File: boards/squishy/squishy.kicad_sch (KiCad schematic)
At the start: 66 parts, among them J10 QXH-060, J2 Conn_02x20_Odd_Even_Shielded, J8 TRIGGER, J9 REFCLK, SW2 DFU, U1 LFE5UM5G-45F-8BG381C, U2 W25N01GVZEIG, U6 ATSAMD09D14A-M, X1 48MHz

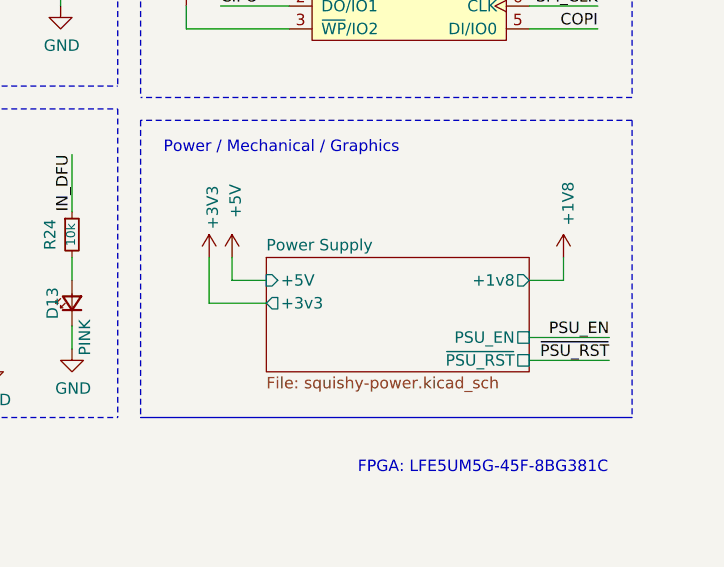
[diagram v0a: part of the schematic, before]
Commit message: hardware: squishy: some more cleanup, as well as starting work on the PSU side of things finally
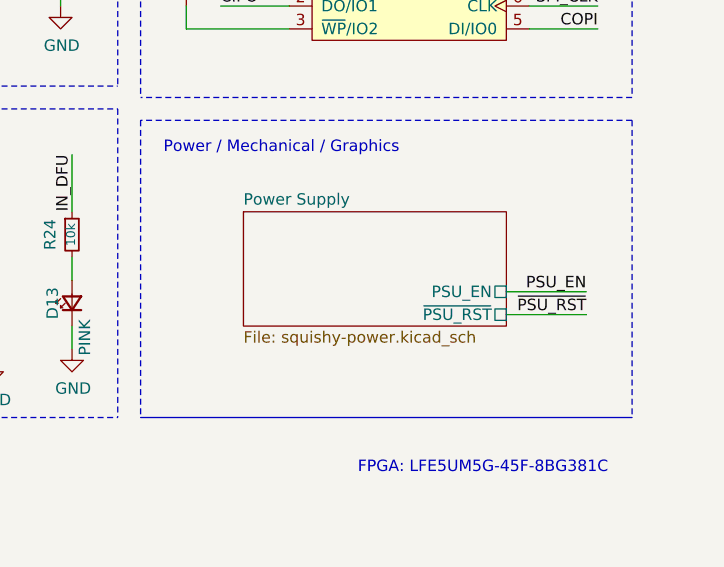
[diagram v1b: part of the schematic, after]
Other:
- sheet Power Supply ports: added none; removed +1v8, +3v3, +5V
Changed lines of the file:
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@@
     (stroke (width 0) (type default) (color 0 0 0 0))
   )
-  (wire (pts (xy 365.76 237.49) (xy 359.41 237.49))
-    (stroke (width 0) (type solid) (color 0 0 0 0))
-  )
   (wire (pts (xy 212.09 257.81) (xy 209.55 257.81))
     (stroke (width 0) (type default) (color 0 0 0 0))
@@
     (stroke (width 0) (type default) (color 0 0 0 0))
   )
-  (wire (pts (xy 361.95 234.95) (xy 365.76 234.95))
-    (stroke (width 0) (type solid) (color 0 0 0 0))
-  )
   (wire (pts (xy 209.55 260.35) (xy 209.55 265.43))
     (stroke (width 0) (type default) (color 0 0 0 0))
@@
     (stroke (width 0) (type default) (color 0 0 0 0))
   )
-  (wire (pts (xy 359.41 232.41) (xy 359.41 237.49))
-    (stroke (width 0) (type solid) (color 0 0 0 0))
-  )
   (wire (pts (xy 378.46 46.99) (xy 364.49 46.99))
     (stroke (width 0) (type solid) (color 0 0 0 0))
@@
     (stroke (width 0) (type default) (color 0 0 0 0))
   )
-  (wire (pts (xy 394.97 241.3) (xy 403.86 241.3))
+  (wire (pts (xy 392.43 236.22) (xy 401.32 236.22))
     (stroke (width 0) (type default) (color 0 0 0 0))
   )
@@
     (stroke (width 0) (type default) (color 0 0 0 0))
   )
-  (wire (pts (xy 394.97 243.84) (xy 403.86 243.84))
+  (wire (pts (xy 392.43 238.76) (xy 401.32 238.76))
     (stroke (width 0) (type default) (color 0 0 0 0))
   )
@@
     (stroke (width 0) (type default) (color 0 0 0 0))
   )
-  (wire (pts (xy 394.97 234.95) (xy 398.78 234.95))
-    (stroke (width 0) (type default) (color 0 0 0 0))
-  )
-  (wire (pts (xy 398.78 234.95) (xy 398.78 232.41))
-    (stroke (width 0) (type default) (color 0 0 0 0))
-  )
   (wire (pts (xy 212.09 252.73) (xy 198.12 252.73))
     (stroke (width 0) (type default) (color 0 0 0 0))
@@
     (stroke (width 0) (type solid) (color 0 0 0 0))
   )
-  (wire (pts (xy 361.95 232.41) (xy 361.95 234.95))
-    (stroke (width 0) (type solid) (color 0 0 0 0))
-  )
   (wire (pts (xy 293.37 127) (xy 293.37 128.27))
     (stroke (width 0) (type default) (color 0 0 0 0))
@@
     (effects (font (size 1.27 1.27)) (justify left bottom))
   )
-  (label "PSU_EN" (at 403.86 241.3 180)
+  (label "PSU_EN" (at 401.32 236.22 180)
     (effects (font (size 1.27 1.27)) (justify right bottom))
   )
@@
     (effects (font (size 1.27 1.27)) (justify right bottom))
   )
-  (label "~{PSU_RST}" (at 403.86 243.84 180)
+  (label "~{PSU_RST}" (at 401.32 238.76 180)
     (effects (font (size 1.27 1.27)) (justify right bottom))
   )
@@
     (pin "2")
   )
-  (symbol (lib_id "power:+3V3") (at 359.41 232.41 0) (unit 1)
-    (in_bom yes) (on_board yes)
-    (property "Reference" "#PWR011" (id 0) (at 359.41 236.22 0)
-      (effects (font (size 1.27 1.27)) hide)
-    )
-    (property "Value" "+3V3" (id 1) (at 359.791 229.2858 90)
-      (effects (font (size 1.27 1.27)) (justify left))
-    )
-    (property "Footprint" "" (id 2) (at 359.41 232.41 0)
-      (effects (font (size 1.27 1.27)) hide)
-    )
-    (property "Datasheet" "" (id 3) (at 359.41 232.41 0)
-      (effects (font (size 1.27 1.27)) hide)
-    )
-    (pin "1")
-  )
   (symbol (lib_id "Device:R_Small") (at 375.92 88.9 0) (mirror y) (unit 1)
     (in_bom yes) (on_board yes)
@@
     (pin "2")
   )
-  (symbol (lib_id "power:+5V") (at 361.95 232.41 0) (unit 1)
-    (in_bom yes) (on_board yes)
-    (property "Reference" "#PWR012" (id 0) (at 361.95 236.22 0)
-      (effects (font (size 1.27 1.27)) hide)
-    )
-    (property "Value" "+5V" (id 1) (at 362.331 228.0158 90)
-      (effects (font (size 1.27 1.27)) (justify left))
-    )
-    (property "Footprint" "" (id 2) (at 361.95 232.41 0)
-      (effects (font (size 1.27 1.27)) hide)
-    )
-    (property "Datasheet" "" (id 3) (at 361.95 232.41 0)
-      (effects (font (size 1.27 1.27)) hide)
-    )
-    (pin "1")
-  )
-  (symbol (lib_id "power:+1V8") (at 398.78 232.41 0) (unit 1)
-    (in_bom yes) (on_board yes)
-    (property "Reference" "#PWR014" (id 0) (at 398.78 236.22 0)
-      (effects (font (size 1.27 1.27)) hide)
-    )
-    (property "Value" "+1V8" (id 1) (at 400.05 228.854 90)
-      (effects (font (size 1.27 1.27)) (justify left bottom))
-    )
-    (property "Footprint" "" (id 2) (at 398.78 232.41 0)
-      (effects (font (size 1.27 1.27)) hide)
-    )
-    (property "Datasheet" "" (id 3) (at 398.78 232.41 0)
-      (effects (font (size 1.27 1.27)) hide)
-    )
-    (pin "1")
-  )
   (symbol (lib_id "power:+3V3") (at 402.59 200.66 0) (unit 1)
     (in_bom yes) (on_board yes)
@@
     (pin "9")
   )
-  (sheet (at 365.76 232.41) (size 29.21 12.7) (fields_autoplaced)
+  (sheet (at 363.22 227.33) (size 29.21 12.7) (fields_autoplaced)
     (stroke (width 0.0006) (type solid) (color 0 0 0 0))
     (fill (color 0 0 0 0.0000))
-    (property "Sheet name" "Power Supply" (id 0) (at 365.76 231.7743 0)
+    (property "Sheet name" "Power Supply" (id 0) (at 363.22 226.6943 0)
       (effects (font (size 1.27 1.27)) (justify left bottom))
     )
-    (property "Sheet file" "squishy-power.kicad_sch" (id 1) (at 365.76 245.6187 0)
+    (property "Sheet file" "squishy-power.kicad_sch" (id 1) (at 363.22 240.5387 0)
       (effects (font (size 1.27 1.27)) (justify left top))
     )
-    (pin "+5V" input (at 365.76 234.95 180)
-      (effects (font (size 1.27 1.27)) (justify left))
-    )
-    (pin "+3v3" output (at 365.76 237.49 180)
-      (effects (font (size 1.27 1.27)) (justify left))
-    )
-    (pin "+1v8" output (at 394.97 234.95 0)
-      (effects (font (size 1.27 1.27)) (justify right))
-    )
-    (pin "~{PSU_RST}" passive (at 394.97 243.84 0)
+    (pin "~{PSU_RST}" passive (at 392.43 238.76 0)
       (effects (font (size 1.27 1.27)) (justify right))
     )
-    (pin "PSU_EN" passive (at 394.97 241.3 0)
+    (pin "PSU_EN" passive (at 392.43 236.22 0)
       (effects (font (size 1.27 1.27)) (justify right))
     )
@@
       (reference "#PWR010") (unit 1) (value "+3V3") (footprint "")
     )
-    (path "/0dfe8ed5-1e00-44b5-8b29-9f19c55853ac"
-      (reference "#PWR011") (unit 1) (value "+3V3") (footprint "")
-    )
-    (path "/812a46ee-0624-409f-bf0d-e79713b4bd3f"
-      (reference "#PWR012") (unit 1) (value "+5V") (footprint "")
-    )
     (path "/135fa4cc-bf68-4ed2-9d1e-cefa9ceb3983/ce342459-d87a-4172-8610-8195b6d3757c"
       (reference "#PWR013") (unit 1) (value "GND") (footprint "")
     )
-    (path "/8279c182-7b45-4e7b-98e9-d407e02d1772"
-      (reference "#PWR014") (unit 1) (value "+1V8") (footprint "")
-    )
     (path "/dee06aeb-8b25-4ab3-8933-7c75dd499370"
       (reference "#PWR020") (unit 1) (value "+3V3") (footprint "")
@@
       (reference "#PWR038") (unit 1) (value "GND") (footprint "")
     )
-    (path "/135fa4cc-bf68-4ed2-9d1e-cefa9ceb3983/e9a9fd75-efc3-4ab5-98ce-6cf265647c3f"
-      (reference "#PWR040") (unit 1) (value "+3V3") (footprint "")
-    )
-    (path "/135fa4cc-bf68-4ed2-9d1e-cefa9ceb3983/8bbdadd5-1e64-497f-ac0d-8c3c8bf7fd8f"
-      (reference "#PWR041") (unit 1) (value "+5V") (footprint "")
-    )
     (path "/135fa4cc-bf68-4ed2-9d1e-cefa9ceb3983/bbc64594-60dc-480d-9780-c1a7ae4ec20f"
       (reference "#PWR042") (unit 1) (value "GND") (footprint "")
     )
-    (path "/135fa4cc-bf68-4ed2-9d1e-cefa9ceb3983/7a9725fa-1e82-4f37-85be-14346fc89c1b"
-      (reference "#PWR043") (unit 1) (value "GND") (footprint "")
-    )
     (path "/135fa4cc-bf68-4ed2-9d1e-cefa9ceb3983/ae107d56-6c6a-46e0-b4ee-ae76a6262fca"
       (reference "#PWR044") (unit 1) (value "+5V") (footprint "")
@@
       (reference "#PWR0114") (unit 1) (value "+3V3") (footprint "")
     )
-    (path "/135fa4cc-bf68-4ed2-9d1e-cefa9ceb3983/de35c65f-a01d-4e76-a55b-53517221bb9b"
-      (reference "#PWR0115") (unit 1) (value "+1V2") (footprint "")
-    )
     (path "/135fa4cc-bf68-4ed2-9d1e-cefa9ceb3983/ae01d070-dcbe-48d1-a6bf-bae5c1d66bea"
       (reference "#PWR0116") (unit 1) (value "+2V5") (footprint "")
     )
-    (path "/135fa4cc-bf68-4ed2-9d1e-cefa9ceb3983/53127b45-6d34-4a35-8652-f009714460fa"
-      (reference "#PWR0117") (unit 1) (value "+2V5") (footprint "")
-    )
     (path "/135fa4cc-bf68-4ed2-9d1e-cefa9ceb3983/83c9ce5e-8c50-463e-8693-7640b1cfd54d"
       (reference "#PWR0118") (unit 1) (value "+2V5") (footprint "")
@@
       (reference "#PWR0120") (unit 1) (value "GND") (footprint "")
     )
-    (path "/135fa4cc-bf68-4ed2-9d1e-cefa9ceb3983/35315390-f586-48e0-8bcd-3c69c794f64a"
-      (reference "#PWR0121") (unit 1) (value "+1V1") (footprint "")
-    )
     (path "/135fa4cc-bf68-4ed2-9d1e-cefa9ceb3983/cd34942c-ad54-4437-ba74-2b44f817dfe1"
       (reference "#PWR0122") (unit 1) (value "+1V2") (footprint "")
@@
       (reference "TP36") (unit 1) (value "COPI") (footprint "TestPoint:TestPoint_Pad_D1.0mm")
     )
+    (path "/135fa4cc-bf68-4ed2-9d1e-cefa9ceb3983/120bb32e-069d-48ff-9f44-be1642520adf"
+      (reference "TP37") (unit 1) (value "1v8") (footprint "TestPoint:TestPoint_Pad_D1.0mm")
+    )
     (path "/135fa4cc-bf68-4ed2-9d1e-cefa9ceb3983/393bcce6-5ec9-4891-87f3-b0b2ec9d858e"
       (reference "U1") (unit 1) (value "LFE5UM5G-45F-8BG381C") (footprint "lethalbit:318caBGA")
@@
     )
     (path "/135fa4cc-bf68-4ed2-9d1e-cefa9ceb3983/3cd17d59-9727-4c74-8a44-5692d0e356fa"
-      (reference "U5") (unit 1) (value "APX811-40UG-7") (footprint "Package_TO_SOT_SMD:SOT-143")
+      (reference "U5") (unit 1) (value "APX811-40UG-7") (footprint "rhais_package-smd:SOT-143")
     )
     (path "/fb4b99fc-1865-483e-9fc3-4bf5e4d53615"

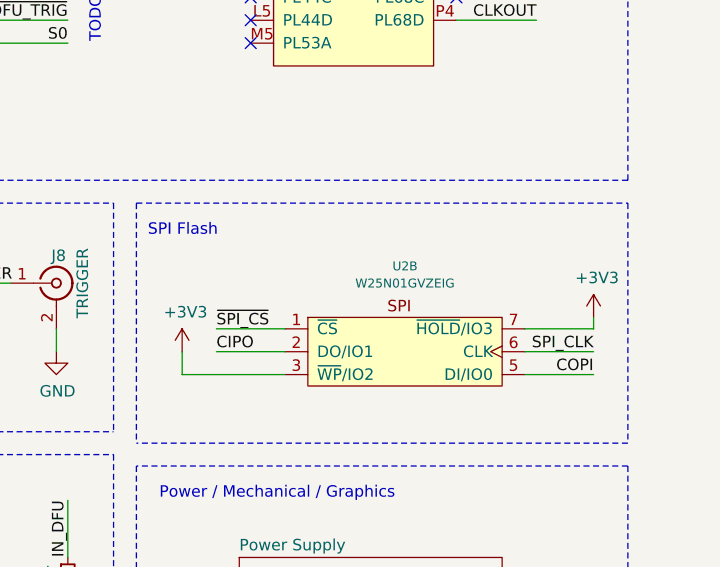
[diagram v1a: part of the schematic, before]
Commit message: hardware: squishy: replaced the SPI flash with a less batshit device from GigaDevice
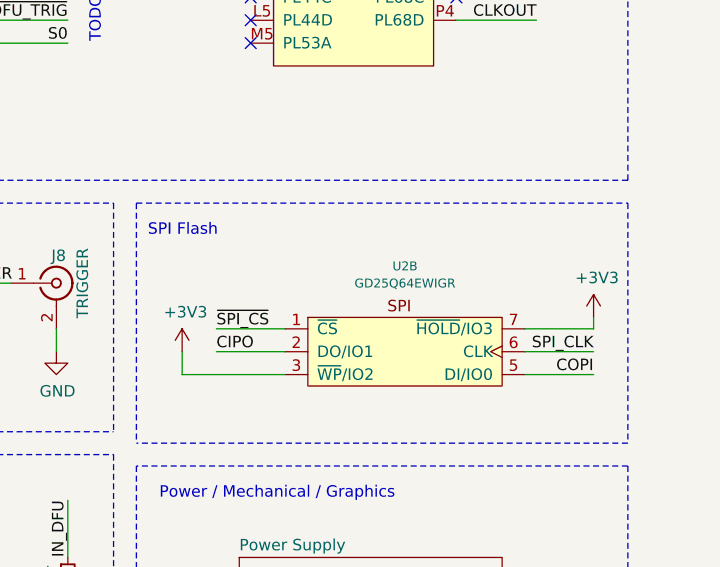
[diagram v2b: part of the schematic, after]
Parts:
- U2: value W25N01GVZEIG -> GD25Q64EWIGR; footprint lethalbit-memory:WSON-8-1EP-6.0x8.0mm -> Package_SON:WSON-8-1EP_6x5mm_P1.27mm_EP3.4x4mm; MFR Winbond -> GigaDevice; MPN W25N01GVZEIG TR -> GD25Q64EWIGR
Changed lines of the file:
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@@
       (effects (font (size 0.9906 0.9906)))
     )
-    (property "Value" "W25N01GVZEIG" (id 1) (at 381.635 196.8754 0)
+    (property "Value" "GD25Q64EWIGR" (id 1) (at 381.635 196.8754 0)
       (effects (font (size 0.9906 0.9906)))
     )
-    (property "Footprint" "lethalbit-memory:WSON-8-1EP-6.0x8.0mm" (id 2) (at 381 196.85 0)
+    (property "Footprint" "Package_SON:WSON-8-1EP_6x5mm_P1.27mm_EP3.4x4mm" (id 2) (at 381 196.85 0)
       (effects (font (size 0.9906 0.9906)) hide)
     )
-    (property "Datasheet" "https://www.winbond.com/resource-files/w25n01gv%20revl%20050918%20unsecured.pdf" (id 3) (at 381 196.85 0)
+    (property "Datasheet" "https://www.gigadevice.com/datasheet/GD25Q64E/" (id 3) (at 381 196.85 0)
       (effects (font (size 0.9906 0.9906)) hide)
     )
-    (property "MFR" "Winbond" (id 4) (at 381 200.66 0)
+    (property "MFR" "GigaDevice" (id 4) (at 381 200.66 0)
       (effects (font (size 1.27 1.27)) hide)
     )
-    (property "MPN" "W25N01GVZEIG TR" (id 5) (at 381 200.66 0)
+    (property "MPN" "GD25Q64EWIGR" (id 5) (at 381 200.66 0)
       (effects (font (size 1.27 1.27)) hide)
     )
@@
     )
     (path "/135fa4cc-bf68-4ed2-9d1e-cefa9ceb3983/44f7f89d-f61a-424b-8f8b-f31a10fe8aec"
-      (reference "U2") (unit 1) (value "W25N01GVZEIG") (footprint "lethalbit-memory:WSON-8-1EP-6.0x8.0mm")
+      (reference "U2") (unit 1) (value "GD25Q64EWIGR") (footprint "Package_SON:WSON-8-1EP_6x5mm_P1.27mm_EP3.4x4mm")
     )
     (path "/00000000-0000-0000-0000-000072b96835"
-      (reference "U2") (unit 2) (value "W25N01GVZEIG") (footprint "lethalbit-memory:WSON-8-1EP-6.0x8.0mm")
+      (reference "U2") (unit 2) (value "GD25Q64EWIGR") (footprint "Package_SON:WSON-8-1EP_6x5mm_P1.27mm_EP3.4x4mm")
     )
     (path "/897376f2-0c69-4736-a5dd-4d1ec77915b7/05f56e17-30f7-48dd-b997-ca5a8f35def9"
